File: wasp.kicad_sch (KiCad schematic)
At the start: 60 parts

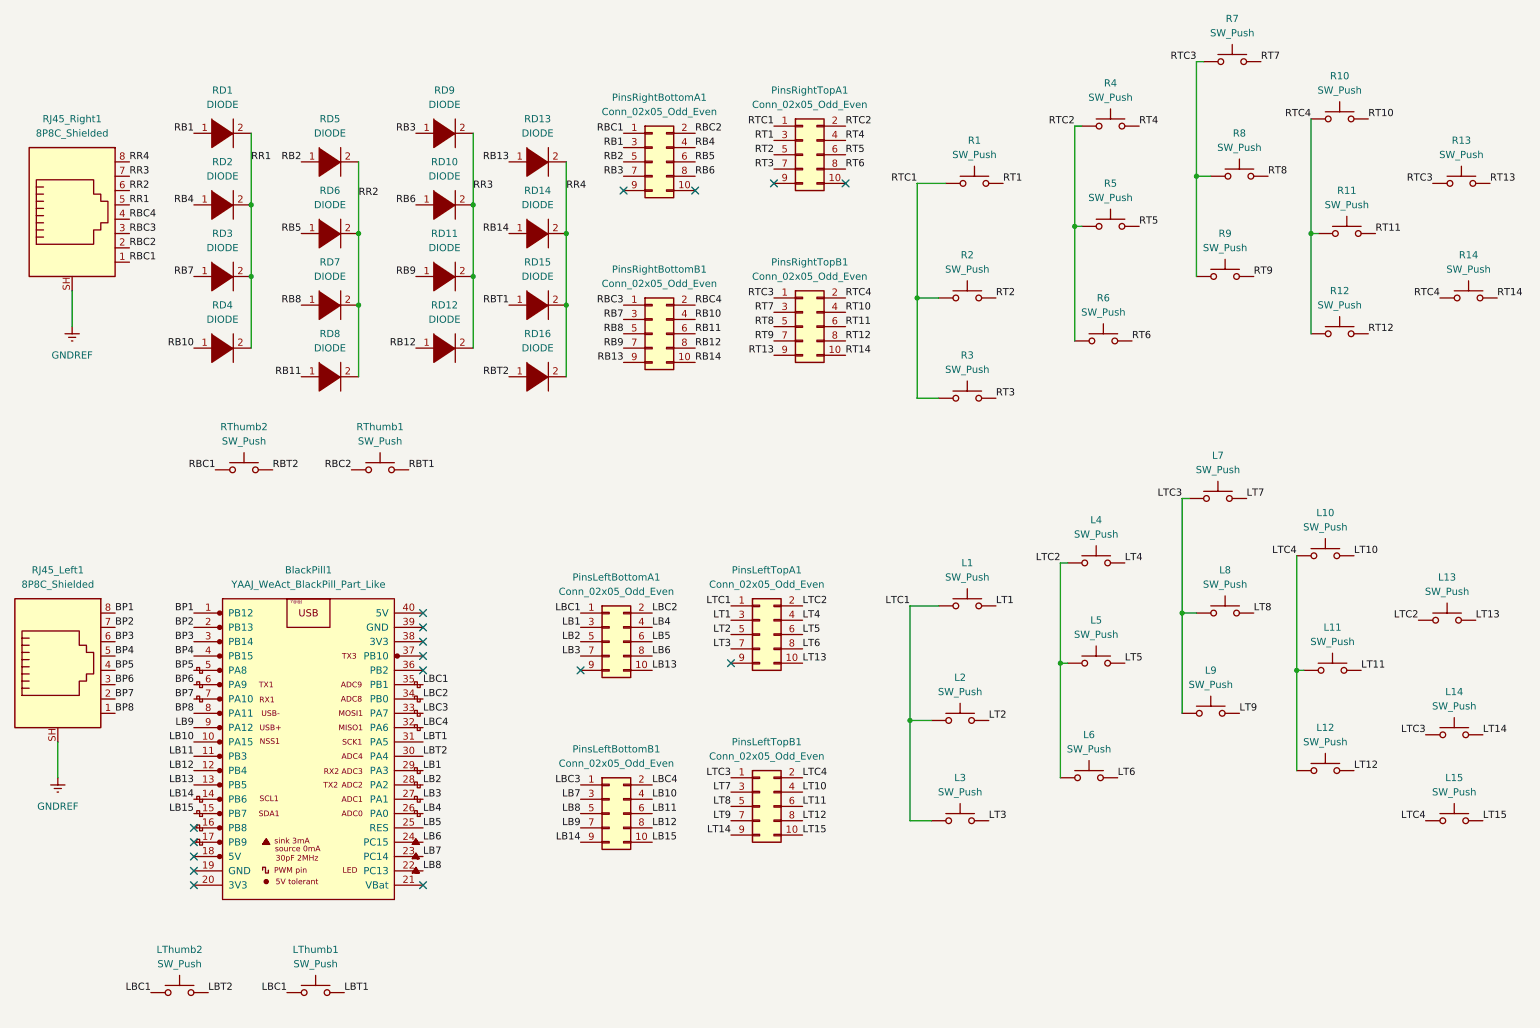
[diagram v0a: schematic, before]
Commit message: Schema finished and ERC passes, removed usage ofunusable pins on blackpill
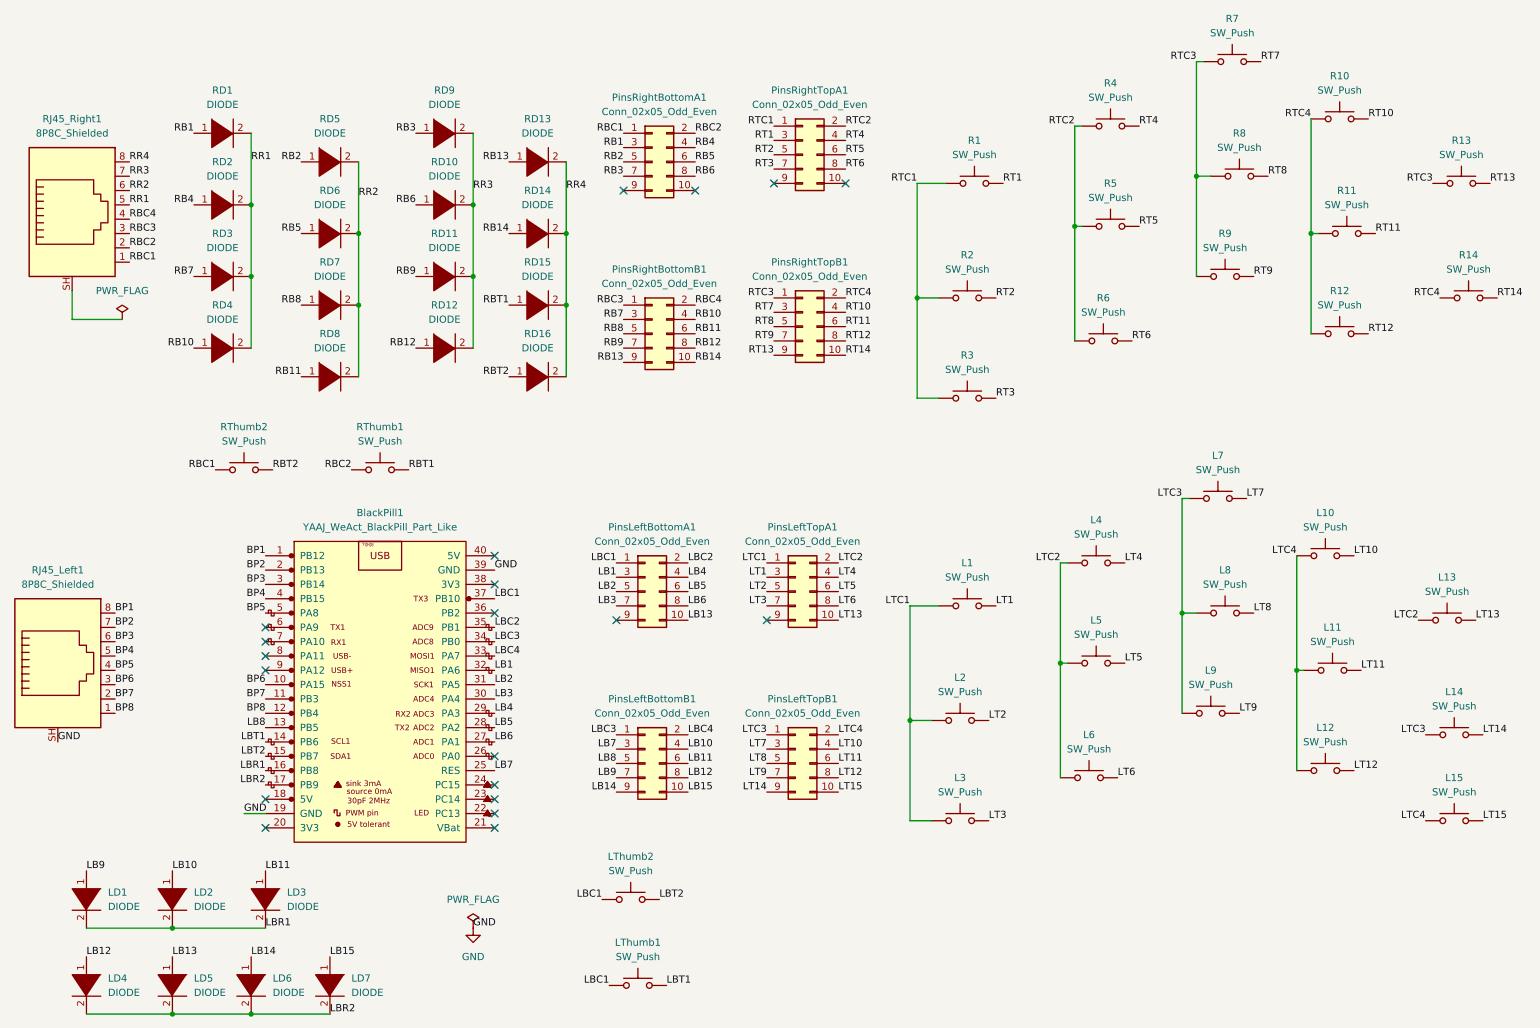
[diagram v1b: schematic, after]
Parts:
- added LD1, LD2, LD3, LD4, LD5, LD6, LD7: DIODE, Diode_THT:D_DO-35_SOD27_P7.62mm_Horizontal, symbol pspice:DIODE
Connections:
- net BP6: now also BlackPill1.10 (PA15); no longer BlackPill1.6 (PA9)
- net BP7: now also BlackPill1.11 (PB3); no longer BlackPill1.7 (PA10)
- net BP8: now also BlackPill1.12 (PB4); no longer BlackPill1.8 (PA11)
- net LB1: now also BlackPill1.32 (PA6); no longer BlackPill1.29 (PA3)
- net LB10: now also LD2.1 (K); no longer BlackPill1.10 (PA15)
- net LB11: now also LD3.1 (K); no longer BlackPill1.11 (PB3)
- net LB12: now also LD4.1 (K); no longer BlackPill1.12 (PB4)
- net LB13: now also LD5.1 (K); no longer BlackPill1.13 (PB5)
- net LB14: now also LD6.1 (K); no longer BlackPill1.14 (PB6)
- net LB15: now also LD7.1 (K); no longer BlackPill1.15 (PB7)
- net LB2: now also BlackPill1.31 (PA5); no longer BlackPill1.28 (PA2)
- net LB3: now also BlackPill1.30 (PA4); no longer BlackPill1.27 (PA1)
- net LB4: now also BlackPill1.29 (PA3); no longer BlackPill1.26 (PA0)
- net LB5: now also BlackPill1.28 (PA2); no longer BlackPill1.25 (RES)
- net LB6: now also BlackPill1.27 (PA1); no longer BlackPill1.24 (PC15)
- net LB7: now also BlackPill1.25 (RES); no longer BlackPill1.23 (PC14)
- net LB8: now also BlackPill1.13 (PB5); no longer BlackPill1.22 (PC13)
- net LB9: now also LD1.1 (K); no longer BlackPill1.9 (PA12)
- net LBC1: now also BlackPill1.37 (PB10); no longer BlackPill1.35 (PB1)
- net LBC2: now also BlackPill1.35 (PB1); no longer BlackPill1.34 (PB0)
- net LBC3: now also BlackPill1.34 (PB0); no longer BlackPill1.33 (PA7)
- net LBC4: now also BlackPill1.33 (PA7); no longer BlackPill1.32 (PA6)
- net LBT1: now also BlackPill1.14 (PB6); no longer BlackPill1.31 (PA5)
- net LBT2: now also BlackPill1.15 (PB7); no longer BlackPill1.30 (PA4)
- net LBR1: now reaches BlackPill1.16 (PB8)
- net LBR1: now also LD1.2 (A), LD2.2 (A), LD3.2 (A)
- net LBR2: now reaches BlackPill1.17 (PB9)
- net LBR2: now also LD4.2 (A), LD5.2 (A), LD6.2 (A), LD7.2 (A)
- net GND: now reaches BlackPill1.19 (GND)
- net GND: now also BlackPill1.39 (GND), RJ45_Left1.SH
- net GNDREF: no longer names the net of RJ45_Right1.SH
- net GNDREF: no longer RJ45_Left1.SH
- no-connect marks 17 -> 20
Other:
- company: (none) -> Appman
- title: (none) -> The Wasp Keyboard
- moved on the sheet: BlackPill1, LThumb1, LThumb2, PinsLeftBottomA1, PinsLeftBottomB1, PinsLeftTopA1, PinsLeftTopB1
